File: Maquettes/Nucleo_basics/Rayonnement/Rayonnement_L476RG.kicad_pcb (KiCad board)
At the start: 2 copper layers, 90 x 92.5 mm, 34 parts, among them J1 LED_IN, J10 GND_reg, J11 3.3V_reg, J2 Servo, J3 POWER_IN, J4 Morpho_Gauche, J5 LED_OUT, J6 PhotoDiode, J7 Morpho_Droite, J8 D_IN_OUT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

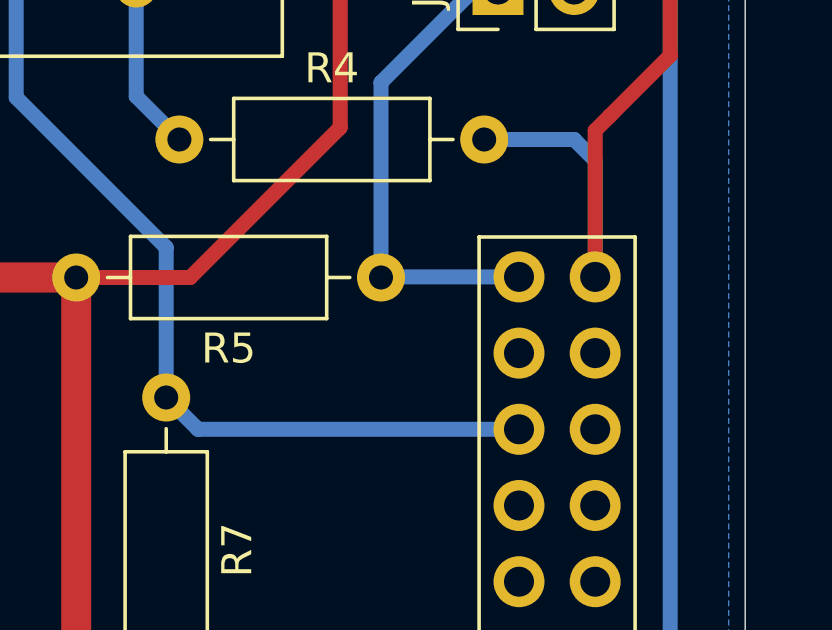
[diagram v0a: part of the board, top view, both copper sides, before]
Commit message: Update Radiation DIagram Board
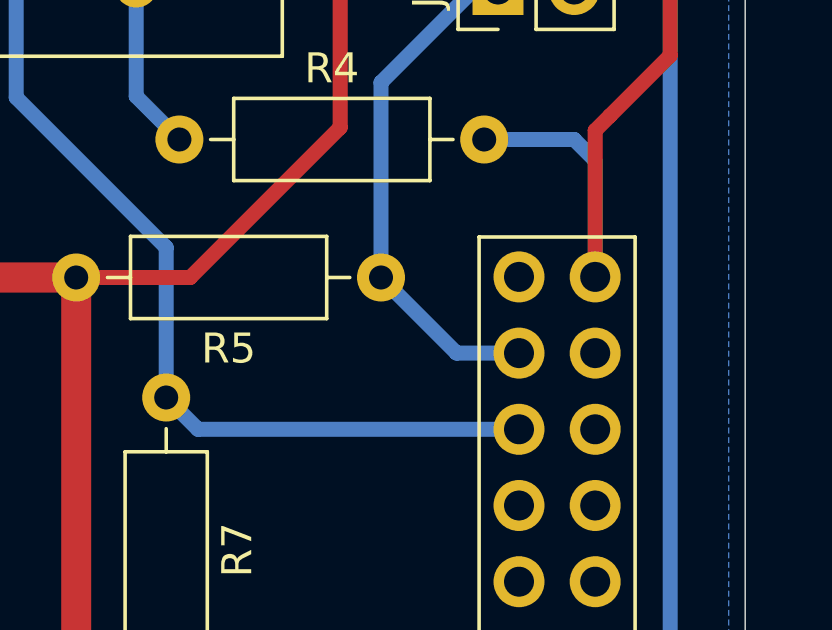
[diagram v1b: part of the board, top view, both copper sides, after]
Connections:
- J4 pad 38: unconnected-(J4-Pin_38-Pad38) -> RT_OUT
- J4 pad 40: RT_OUT -> unconnected-(J4-Pin_40-Pad40)
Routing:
- net RT_OUT: track 16.3 -> 17.4 mm
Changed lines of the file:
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@@
 	(net 6 "LED_POW_IN")
 	(net 7 "unconnected-(J4-Pin_6-Pad6)")
-	(net 8 "unconnected-(J4-Pin_38-Pad38)")
+	(net 8 "unconnected-(J4-Pin_40-Pad40)")
 	(net 9 "unconnected-(J4-Pin_35-Pad35)")
 	(net 10 "unconnected-(J4-Pin_1-Pad1)")
@@
 			(layers "*.Cu" "*.Mask")
 			(remove_unused_layers no)
-			(net 8 "unconnected-(J4-Pin_38-Pad38)")
+			(net 35 "RT_OUT")
 			(pinfunction "Pin_38")
 			(pintype "passive")
@@
 			(layers "*.Cu" "*.Mask")
 			(remove_unused_layers no)
-			(net 35 "RT_OUT")
+			(net 8 "unconnected-(J4-Pin_40-Pad40)")
 			(pinfunction "Pin_40")
 			(pintype "passive")
@@
 	)
 	(segment
-		(start 205.96 95.18)
-		(end 201.38 95.18)
+		(start 203.88 97.72)
+		(end 205.96 97.72)
+		(width 0.5)
+		(layer "B.Cu")
+		(net 35)
+	)
+	(segment
+		(start 201.36 95.2)
+		(end 203.88 97.72)
 		(width 0.5)
 		(layer "B.Cu")
